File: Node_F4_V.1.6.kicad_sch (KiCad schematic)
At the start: 171 parts, among them IC2 MP1584EN, J2 Conn_02x12_Odd_Even, J3 Micro_SD_Card, J4 RF_IPEX_U.FL-R-SMT, J5 Conn_01x06, J5 LoRa_Anten, J6 Conn_01x06, J7 RS485, J8 Conn_Jack-DC, Q1 BC847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

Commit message: DI track
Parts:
- removed C1: 10uF, Anh_Footprints:C_0603, symbol Device:C
- removed C2: 1uF, Anh_Footprints:C_0603, symbol Device:C
- removed C50: 5.6pF, Anh_Footprints:C_0603, symbol Device:C_Small
- removed C54: 100nF, Anh_Footprints:C_0603, symbol Device:C_Small
- removed R46: TBD, Anh_Footprints:R_0603, symbol Device:R
- removed Z1: D_Zener, IVS_FOOTPRINTS:D_MiniMELF, symbol IVS_SYMBOLS:D_Zener
- added C39: NC, Anh_Footprints:C_0603, symbol Device:C_Small
- added C89: 100nF, Anh_Footprints:C_0603, symbol Device:C_Small
- added R23: 10K, Anh_Footprints:R_0603, symbol Device:R
- C51: value 2.4pF -> NC
- C77, C78: value 6.8pF -> NC
- D9, Q1, Q2: footprint IVS_FOOTPRINTS:SOT23-3 -> Anh_Footprints:SOT23-3
- J2: value Conn_02x12_Odd_Even -> IDC_LCD_KEYPAD
- J4: footprint Connector_Coaxial:U.FL_Hirose_U.FL-R-SMT-1_Vertical -> Anh_Footprints:IPEX_Antena_Connector
- J5: value Conn_01x06 -> SWD
- J6: value Conn_01x06 -> WiFi_Prog
- L4: value 2.7nH -> 2.2nH
- U4: footprint Package_SO:SOIC-8_5.23x5.23mm_P1.27mm -> Anh_Footprints:SOIC-8_5.23x5.23
- U5: footprint IVS_FOOTPRINTS:SOIC-16W_7.5x10.3mm_P1.27mm -> Package_SO:SOIC-16W_7.5x10.3mm_P1.27mm
- Y1, Y2: footprint IVS_FOOTPRINTS:Crystal_SMD_5032-4Pin_5.0x3.2mm -> Anh_Footprints:Crystal_3225_4P_1-4
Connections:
- net +3.3V: now also C89.1
- net A+: now also J7.1 (Pin_1); no longer J7.2 (Pin_2)
- net B-: now also J7.2 (Pin_2); no longer J7.3 (Pin_3)
- net BUZZER: now also U3.71 (PA12); no longer U3.1 (PE2)
- net GND: now also J7.3 (Pin_3), C39.2, C89.2, R23.2; no longer J7.1 (Pin_1), L4.2
- net SWCLK: now also U3.76 (PA14)
- net SWDIO: now also U3.72 (PA13)
- net at C51.1, J4.1 (In): now also L4.1
- net at U3.7 (PC13): now also D1.2 (A)
- net at U3.9 (PC15): no longer D1.2 (A)
- net at Q2.1 (B), R42.1: now also R23.1
- net at C45.2, Y2.1: now also U6.45 (XTAL_P)
- net at U6.2 (LNA_IN): now also L4.2, C39.1; no longer L4.1
- no-connect marks 4 -> 27
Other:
- note added: "LoRa"
- note added: "RS485"
- note added: "RTC"
- note added: "SD Card"
- note added: "STM32"
- note removed: "DS3231"
- note removed: "LORA"
- moved on the sheet: BT1, BZ1, C10, C100, C101, C102, C11, C12, C19, C2, C21, C22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

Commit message: 50%
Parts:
- removed C89: 100nF, Anh_Footprints:C_0603, symbol Device:C_Small
- removed D1: LED_Blink, Anh_Footprints:LED_0603, symbol Device:LED
- removed J2: IDC_LCD_KEYPAD, Connector_IDC:IDC-Header_2x12_P2.54mm_Vertical, symbol Connector_Generic:Conn_02x12_Odd_Even
- removed J3: Micro_SD_Card, Anh_Footprints:MicroSD_Socket_9P, symbol Connector:Micro_SD_Card
- removed R10, R11, R12, R13, R9: 10k, Anh_Footprints:R_0603, symbol Device:R_Small
- removed R13: 470, Anh_Footprints:R_0603, symbol Device:R_Small
- added C50: 1u, Anh_Footprints:C_0603, symbol Device:C_Small
- added C54: 100n, Anh_Footprints:C_0603, symbol Device:C_Small
- added D15 (x4): LED, Anh_Footprints:LED_0603, symbol Device:LED
- added J2: Conn_01x10, IVS_FOOTPRINTS:XH 2.54 10Pin Female, symbol Connector_Generic:Conn_01x10
- added J3: Conn_01x16_Female, Connector_PinSocket_2.54mm:PinSocket_1x16_P2.54mm_Vertical, symbol Connector:Conn_01x16_Female
- added Q1: P_Mosfet, Anh_Footprints:SOT23-3, symbol IVS_Symbol:P_Mosfet
- added R24: 1M, Anh_Footprints:R_0603, symbol Device:R
- added R27 (x4): 220, Anh_Footprints:R_0603, symbol Device:R_Small
- added U7: W25Q128JVS, IVS_FOOTPRINTS:SOIC-8_5.23x5.23mm_P1.27mm, symbol Memory_Flash:W25Q128JVS
- C97: footprint Anh_Footprints:C_0603 -> Anh_Footprints:C_1210
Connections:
- net +3.3V: now also C50.2, C54.2, D15.2 (A), D15.2 (A), D15.2 (A), D15.2 (A), J3.2 (Pin_2), U7.3 (IO2), U7.7 (IO3), U7.8 (VCC)
- net BUZZER: now also U3.48 (PB11); no longer U3.71 (PA12)
- net GND: now also C50.1, C54.1, J3.1 (Pin_1), Q1.2 (S), R24.1, U7.4 (GND)
- net SPI_MISO: now also U7.2 (DO(IO1))
- net SPI_MOSI: now also U7.5 (DI(IO0))
- net SPI_SCK: now also U7.6 (CLK)
- net TFT_CS: now also U3.5 (PE6), J3.3 (Pin_3)
- net TFT_DB0: now also U3.39 (PE8), J3.9 (Pin_9)
- net TFT_DB1: now also U3.40 (PE9), J3.10 (Pin_10)
- net TFT_DB2: now also U3.41 (PE10), J3.11 (Pin_11)
- net TFT_DB3: now also U3.42 (PE11), J3.12 (Pin_12)
- net TFT_DB4: now also U3.43 (PE12), J3.13 (Pin_13)
- net TFT_DB5: now also U3.44 (PE13), J3.14 (Pin_14)
- net TFT_DB6: now also U3.45 (PE14), J3.15 (Pin_15)
- net TFT_DB7: now also U3.46 (PE15), J3.16 (Pin_16)
- net TFT_LED: now also U3.98 (PE1), Q1.1 (G), R24.2
- net TFT_RD: now also U3.2 (PE3), J3.6 (Pin_6)
- net TFT_RS: now also U3.4 (PE5), J3.4 (Pin_4)
- net TFT_RST: now also U3.1 (PE2), J3.7 (Pin_7)
- net TFT_WR: now also U3.3 (PE4), J3.5 (Pin_5)
- net W25Q_CS: now reaches U3.51 (PB12)
- net W25Q_CS: now also U7.1 (~{CS})
- net H1: now reaches U3.77 (PA15)
- net H1: now also J2.6 (Pin_6)
- net C4: now reaches U3.81 (PD0)
- net C4: now also J2.5 (Pin_5), R27.2
- net C3: now reaches U3.82 (PD1)
- net C3: now also J2.4 (Pin_4), R27.2
- net C1: now reaches U3.84 (PD3)
- net C1: now also J2.2 (Pin_2), R27.2
- net SD_CLK renamed H4
- net H4: now also J2.9 (Pin_9)
- net SD_CMD renamed C2
- net C2: now also J2.3 (Pin_3), R27.2
- net SD_D0: no longer names the net of U3.65 (PC8)
- net SD_D1: no longer names the net of U3.66 (PC9)
- net SD_D2 renamed H2
- net H2: now also J2.7 (Pin_7)
- net SD_D3 renamed H3
- net H3: now also J2.8 (Pin_8)
- new net: D15.1 (K), R27.1 (x4)
- new net: J3.8 (Pin_8), Q1.3 (D)
- no-connect marks 27 -> 29
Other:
- note added: "FLASH"
- note removed: "SD Card"

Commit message: Xep linh kien
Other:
- moved on the sheet: D15, J2, R27

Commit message: Layout gan xong
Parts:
- added R27 (x4): 1k, Anh_Footprints:R_0603, symbol Device:R_Small
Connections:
- net +3.3V: now also J5.3 (Pin_3), J6.3 (Pin_3), R27.1, R27.1, R27.1, R27.1; no longer J5.4 (Pin_4), J6.4 (Pin_4)
- net BUZZER: no longer U3.48 (PB11)
- net C1: now also U3.31 (PA6), R27.2; no longer U3.84 (PD3)
- net C2: now also U3.32 (PA7), R27.2; no longer U3.83 (PD2)
- net C3: now also U3.33 (PC4), R27.2; no longer U3.82 (PD1)
- net C4: now also U3.34 (PC5), R27.2; no longer U3.81 (PD0)
- net ESP_BOOT: now also J6.1 (Pin_1); no longer J6.6 (Pin_6)
- net ESP_RST: now also J6.2 (Pin_2); no longer J6.5 (Pin_5)
- net ESP_RX: now also U3.25 (PA2); no longer U3.68 (PA9)
- net ESP_RX_LOAD: now also J6.5 (Pin_5); no longer J6.2 (Pin_2)
- net ESP_TX: now also U3.26 (PA3); no longer U3.69 (PA10)
- net ESP_TX_LOAD: now also J6.6 (Pin_6); no longer J6.1 (Pin_1)
- net GND: now also J5.4 (Pin_4), J6.4 (Pin_4); no longer J5.3 (Pin_3), J6.3 (Pin_3)
- net H1: now also U3.35 (PB0); no longer U3.77 (PA15)
- net H2: now also U3.36 (PB1); no longer U3.78 (PC10)
- net H3: now also U3.37 (PB2); no longer U3.79 (PC11)
- net H4: now also U3.38 (PE7); no longer U3.80 (PC12)
- net I2C_SCL: now also U3.47 (PB10); no longer U3.92 (PB6)
- net I2C_SDA: now also U3.48 (PB11); no longer U3.93 (PB7)
- net LORA NSS: now also U3.92 (PB6); no longer U3.55 (PD8)
- net LORA_RST: now also U3.86 (PD5); no longer U3.62 (PD15)
- net RS485_DERE: now also U3.82 (PD1); no longer U3.25 (PA2)
- net RS485_DI: now also U3.80 (PC12); no longer U3.23 (PA0)
- net RS485_RO: now also U3.83 (PD2); no longer U3.24 (PA1)
- net SWCLK: now also J5.6 (Pin_6); no longer J5.1 (Pin_1)
- net SWDIO: now also J5.5 (Pin_5); no longer J5.2 (Pin_2)
- net UART_RX_LOG: now also J5.1 (Pin_1), U3.69 (PA10); no longer J5.6 (Pin_6), U3.87 (PD6)
- net UART_TX_LOG: now also J5.2 (Pin_2), U3.68 (PA9); no longer J5.5 (Pin_5), U3.86 (PD5)
- net W25Q_CS: now also U3.55 (PD8); no longer U3.51 (PB12)
- net SPI3_SCK: now reaches U3.89 (PB3)
- net SPI3_SCK: now also U5.16 (SCK)
- net SPI3_MISO: now reaches U3.90 (PB4)
- net SPI3_MISO: now also U5.17 (MISO)
- net SPI3_MOSI: now reaches U3.91 (PB5)
- net SPI3_MOSI: now also U5.18 (MOSI)
- net LORA_DIO0: no longer names the net of U3.61 (PD14)
- net LORA_DIO0: no longer U5.8 (DIO0)
- net LORA_DIO1: no longer names the net of U3.60 (PD13)
- net LORA_DIO1: no longer U5.9 (DIO1)
- net SPI_MISO renamed SPI2_MISO
- net SPI2_MISO: no longer U5.17 (MISO)
- net SPI_MOSI renamed SPI2_MOSI
- net SPI2_MOSI: no longer U5.18 (MOSI)
- net SPI_SCK renamed SPI2_SCK
- net SPI2_SCK: no longer U5.16 (SCK)
- new net LORA_INT: U3.84 (PD3), U5.8 (DIO0)

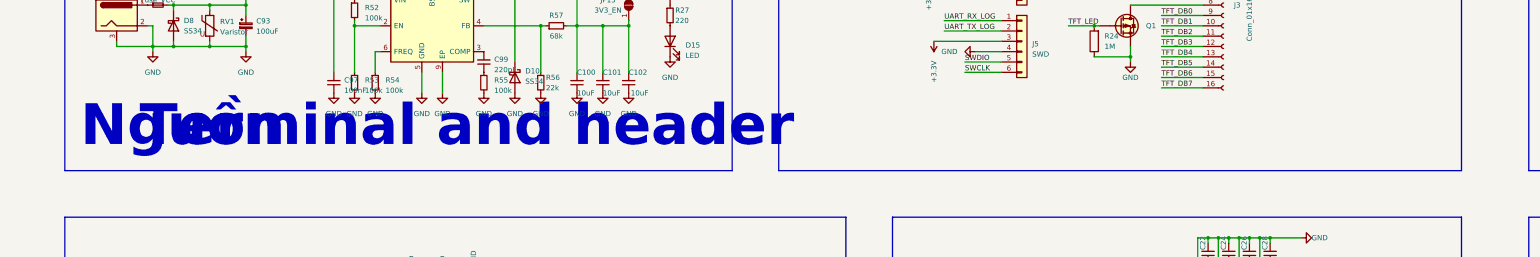
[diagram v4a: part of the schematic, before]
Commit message: Via not foundand connect  GND
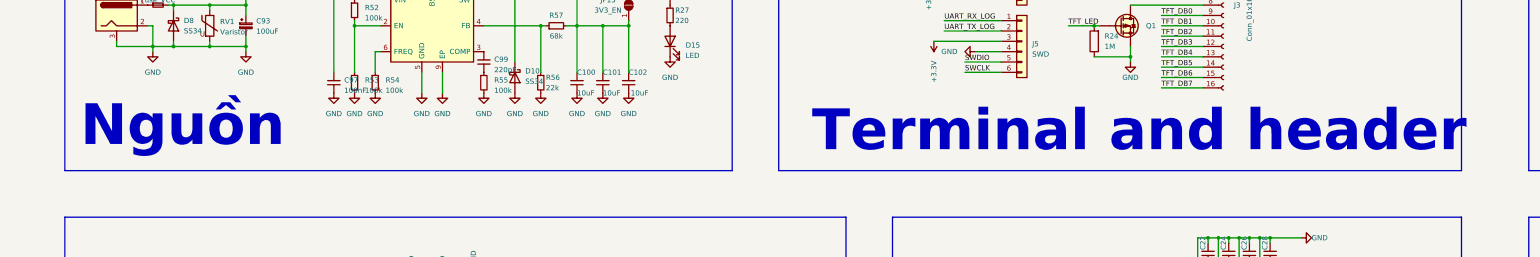
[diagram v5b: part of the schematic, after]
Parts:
- H1, H2, H3, H4: footprint MountingHole:MountingHole_2.2mm_M2_Pad_Via -> MountingHole:MountingHole_2.5mm_Pad_Via
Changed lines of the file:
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@@
     (effects (font (size 10 10) bold (color 204 102 0 1)) (justify left bottom))
   )
-  (text "Terminal and header " (at 248.92 97.79 0)
+  (text "Terminal and header " (at 414.02 99.06 0)
     (effects (font (size 10 10) bold) (justify right bottom))
   )
@@
       (effects (font (size 1.27 1.27)) (justify left))
     )
-    (property "Footprint" "MountingHole:MountingHole_2.2mm_M2_Pad_Via" (at 471.17 332.74 0)
+    (property "Footprint" "MountingHole:MountingHole_2.5mm_Pad_Via" (at 471.17 332.74 0)
       (effects (font (size 1.27 1.27)) hide)
     )
@@
       (effects (font (size 1.27 1.27)) (justify left))
     )
-    (property "Footprint" "MountingHole:MountingHole_2.2mm_M2_Pad_Via" (at 471.17 325.12 0)
+    (property "Footprint" "MountingHole:MountingHole_2.5mm_Pad_Via" (at 471.17 325.12 0)
       (effects (font (size 1.27 1.27)) hide)
     )
@@
       (effects (font (size 1.27 1.27)) (justify left))
     )
-    (property "Footprint" "MountingHole:MountingHole_2.2mm_M2_Pad_Via" (at 471.17 317.5 0)
+    (property "Footprint" "MountingHole:MountingHole_2.5mm_Pad_Via" (at 471.17 317.5 0)
       (effects (font (size 1.27 1.27)) hide)
     )
@@
       (effects (font (size 1.27 1.27)) (justify left))
     )
-    (property "Footprint" "MountingHole:MountingHole_2.2mm_M2_Pad_Via" (at 471.17 340.36 0)
+    (property "Footprint" "MountingHole:MountingHole_2.5mm_Pad_Via" (at 471.17 340.36 0)
       (effects (font (size 1.27 1.27)) hide)
     )

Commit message: Xong layout cho var
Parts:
- added G1: LOGO, Anh_Footprints:MU_Footprint, symbol MU:LOGO
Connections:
- net BUZZER: now also U3.24 (PA1)
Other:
- note added: "KEYPAD"
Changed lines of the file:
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@@
+    (stroke (width 0) (type default))
+  )
+  (wire (pts (xy 384.81 149.86) (xy 378.46 149.86))
     (stroke (width 0) (type default))
   )
@@
   (wire (pts (xy 355.6 119.38) (xy 355.6 120.65))
     (stroke (width 0) (type default))
+  )
+  (rectangle (start 285.75 369.57) (end 414.02 405.13)
+    (stroke (width 0) (type default))
+    (fill (type none))
   )
   (text "FLASH" (at 459.74 57.15 0)
@@
     (effects (font (size 10 10) bold) (justify left bottom))
   )
+  (text "KEYPAD\n" (at 288.29 402.59 0)
+    (effects (font (size 8 8) bold) (justify left bottom))
+  )
   (text "RS485" (at 434.34 193.04 0)
     (effects (font (size 10 10) bold) (justify left bottom))
@@
   (label "SHD_SD2" (at 208.28 186.69 0) (fields_autoplaced)
     (effects (font (size 1.27 1.27)) (justify left bottom))
+  )
+  (label "BUZZER" (at 384.81 149.86 180) (fields_autoplaced)
+    (effects (font (size 1.27 1.27)) (justify right bottom))
   )
   (label "C2" (at 358.14 397.51 0) (fields_autoplaced)
@@
         )
       )
+    )
+  )
+  (symbol (lib_id "MU:LOGO") (at 558.8 40.64 0) (unit 1)
+    (in_bom yes) (on_board yes) (dnp no) (fields_autoplaced)
+    (property "Reference" "G1" (at 558.8 16.2455 0)
+      (effects (font (size 1.27 1.27)) hide)
+    )
+    (property "Value" "LOGO" (at 558.8 65.0345 0)
+      (effects (font (size 1.27 1.27)) hide)
+    )
+    (property "Footprint" "Anh_Footprints:MU_Footprint" (at 558.8 40.64 0)
+      (effects (font (size 1.27 1.27)) hide)
+    )
+    (property "Datasheet" "" (at 558.8 40.64 0)
+      (effects (font (size 1.27 1.27)) hide)
+    )
+    (instances
+      (project "Node_F4_V.1.6"
+        (path "/97356ef2-8252-4a32-a254-d576e058a999"
+          (reference "G1") (unit 1)
+        )
+      )
